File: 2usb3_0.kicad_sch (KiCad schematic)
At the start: 11 parts, among them J5 2xUSB3.0, U3 AP22615AWU

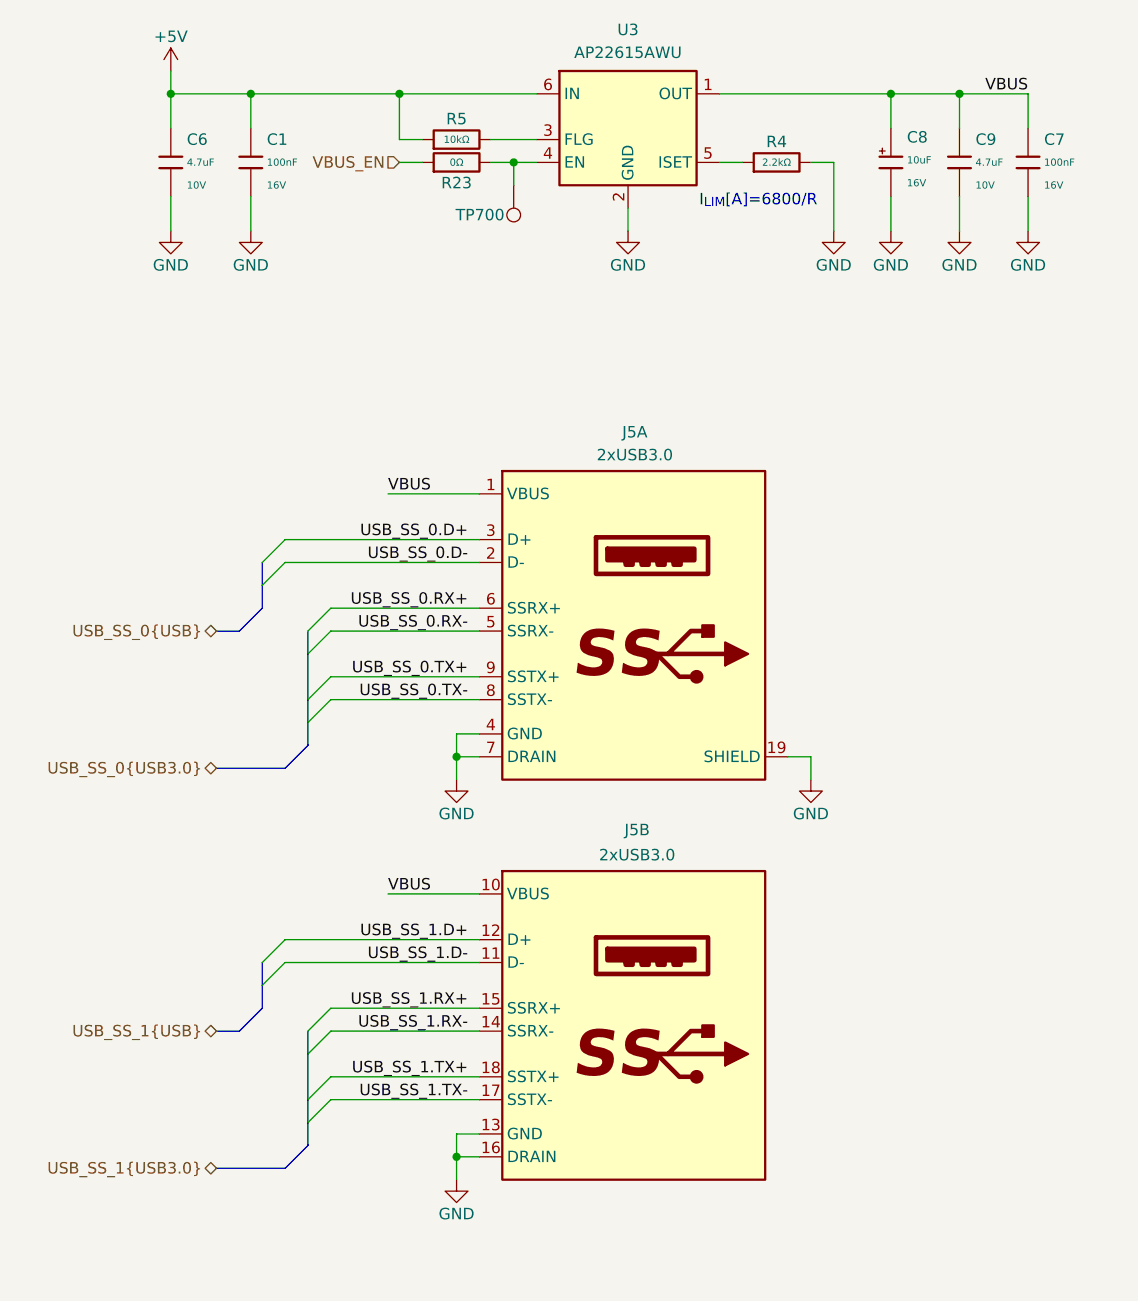
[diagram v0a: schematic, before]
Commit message: [#1] WIP: Change components to ones from the global library, refactor schematic
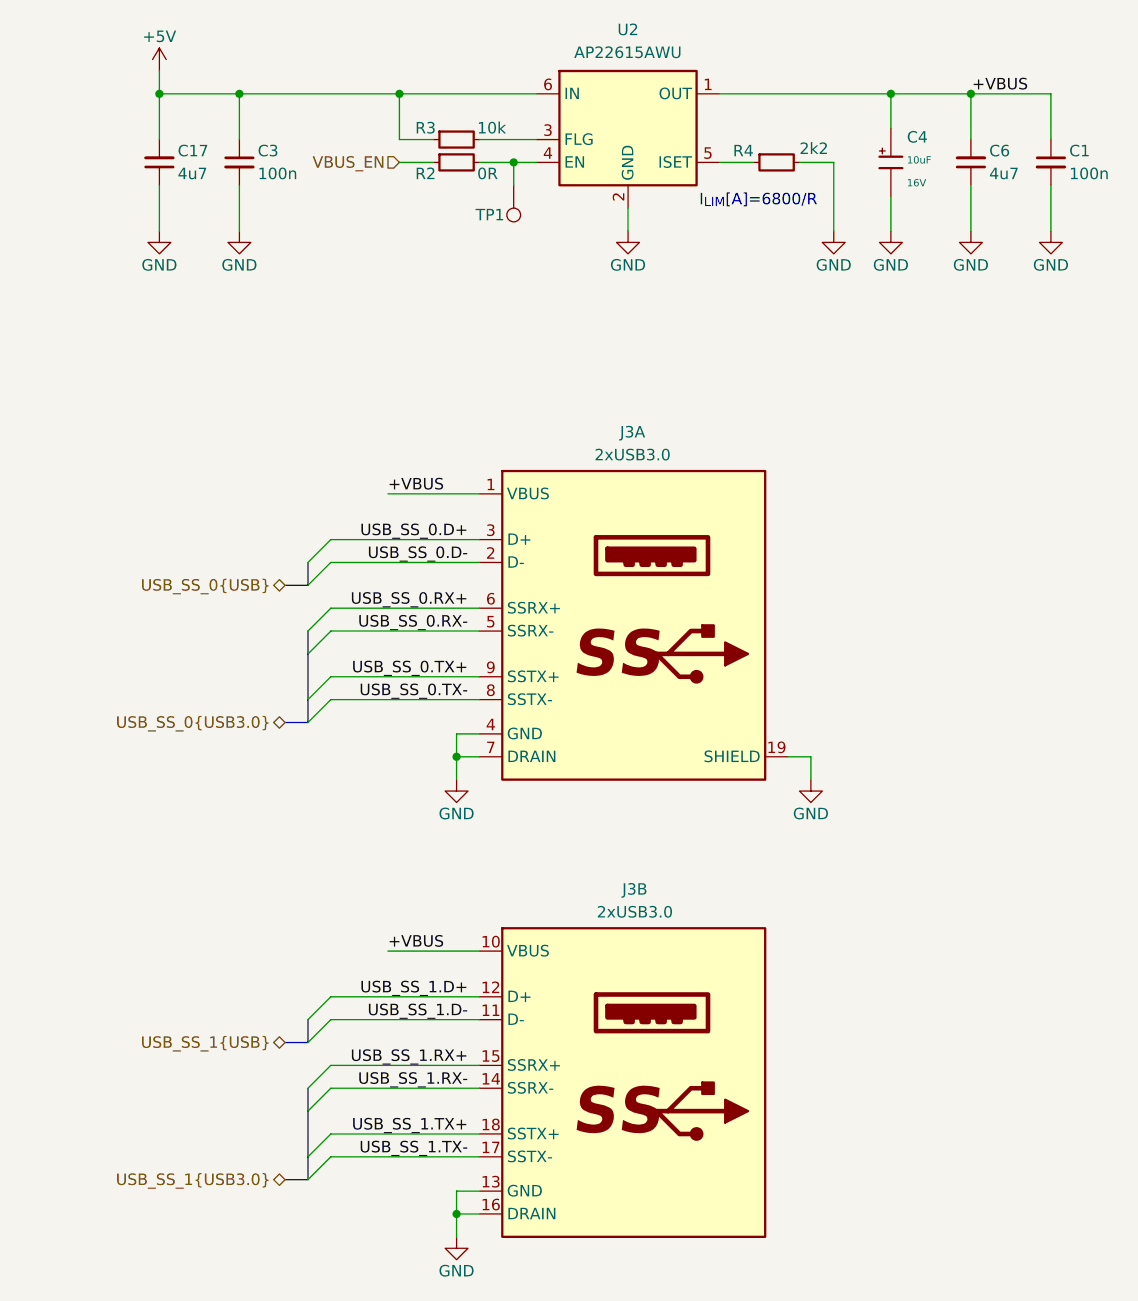
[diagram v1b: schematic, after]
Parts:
- removed C1, C7: 100nF, PCM_JLCPCB:C_0402, symbol PCM_JLCPCB-Capacitors:0402,100nF
- removed C6, C9: 4.7uF, PCM_JLCPCB:C_0402, symbol PCM_JLCPCB-Capacitors:0402,4.7uF
- removed J5: 2xUSB3.0, lib:2xUSB3.0-USB-303WSD-BRY, symbol connectors:2xUSB3.0-USB-303WSD-BRY
- removed R23: 0Ω, PCM_JLCPCB:R_0402, symbol PCM_JLCPCB-Resistors:0402,0Ω
- removed R4: 2.2kΩ, PCM_JLCPCB:R_0402, symbol PCM_JLCPCB-Resistors:0402,2.2kΩ
- removed R5: 10kΩ, PCM_JLCPCB:R_0402, symbol PCM_JLCPCB-Resistors:0402,10kΩ
- added C1, C3: C-100n-0402, DW-footprints:C_0402_1005Metric, symbol DW-capacitors:C-100n-0402
- added C17, C6: C-4u7-0402, DW-footprints:C_0402_1005Metric, symbol DW-capacitors:C-4u7-0402
- added J3: 2xUSB3.0, DW-footprints:2xUSB3.0_USB-303WSD-BRY, symbol DW-connectors:2xUSB3.0_USB-303WSD-BRY
- added R2: R-0R-0402, DW-footprints:R_0402_1005Metric, symbol DW-resistors:R-0R-0402
- added R3: R-10k-0402, DW-footprints:R_0402_1005Metric, symbol DW-resistors:R-10k-0402
- added R4: R-2k2-0402, DW-footprints:R_0402_1005Metric, symbol DW-resistors:R-2k2-0402
- renumbered C8 to C4, TP700 to TP1, U3 to U2
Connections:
- net +5V: now also C17.2, C3.1, R3.1
- net GND: now also C1.2, C17.1, C3.2, C6.1, J3.13 (GND), J3.16 (DRAIN), J3.19 (SHIELD), J3.4 (GND), J3.7 (DRAIN), R4.2
- net USB_SS_0.D+: now also J3.3 (D+)
- net USB_SS_0.D-: now also J3.2 (D-)
- net USB_SS_0.RX+: now also J3.6 (SSRX+)
- net USB_SS_0.RX-: now also J3.5 (SSRX-)
- net USB_SS_0.TX+: now also J3.9 (SSTX+)
- net USB_SS_0.TX-: now also J3.8 (SSTX-)
- net USB_SS_1.D+: now also J3.12 (D+)
- net USB_SS_1.D-: now also J3.11 (D-)
- net USB_SS_1.RX+: now also J3.15 (SSRX+)
- net USB_SS_1.RX-: now also J3.14 (SSRX-)
- net USB_SS_1.TX+: now also J3.18 (SSTX+)
- net USB_SS_1.TX-: now also J3.17 (SSTX-)
- net VBUS_EN: now also R2.1
- net at TP1.1, U2.4 (EN): now also R2.2
- net at U2.3 (FLG): now also R3.2
- net at U2.5 (ISET): now also R4.1
- net VBUS renamed +VBUS
- net +VBUS: now also C1.1, C6.2, J3.1 (VBUS), J3.10 (VBUS)
